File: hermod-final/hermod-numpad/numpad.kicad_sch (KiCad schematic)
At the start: 46 parts

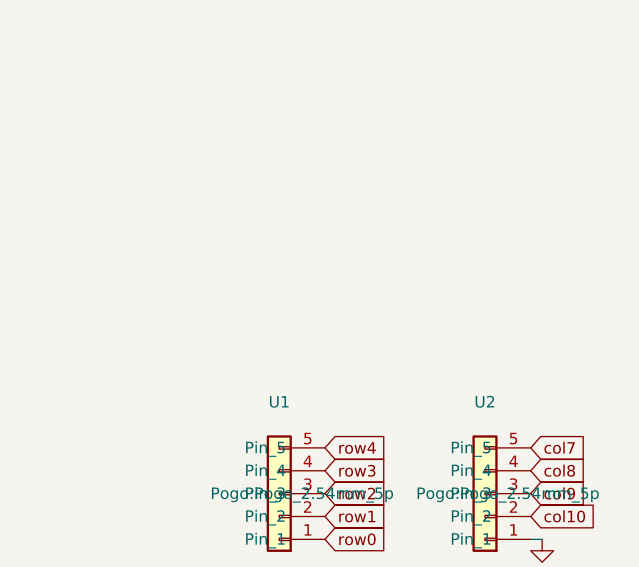
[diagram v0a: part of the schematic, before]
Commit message: Fixed random trace on numpad
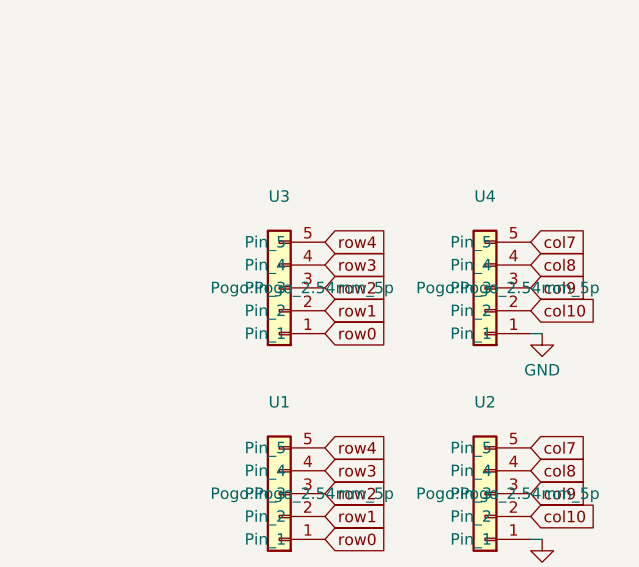
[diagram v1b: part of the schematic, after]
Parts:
- added U3, U4: ~, Pogo:Pogo_2.54mm_5p, symbol Pogo:Pogo_2.54mm_5p
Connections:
- net GND: now also U4.1 (Pin_1)
- net col10: now also U4.2 (Pin_2)
- net col7: now also U4.5 (Pin_5)
- net col8: now also U4.4 (Pin_4)
- net col9: now also U4.3 (Pin_3)
- net row0: now also U3.1 (Pin_1)
- net row1: now also U3.2 (Pin_2)
- net row2: now also U3.3 (Pin_3)
- net row3: now also U3.4 (Pin_4)
- net row4: now also U3.5 (Pin_5)
